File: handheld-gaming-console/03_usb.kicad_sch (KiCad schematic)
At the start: 16 parts, among them U6 USB2514B, Y1 24MHz

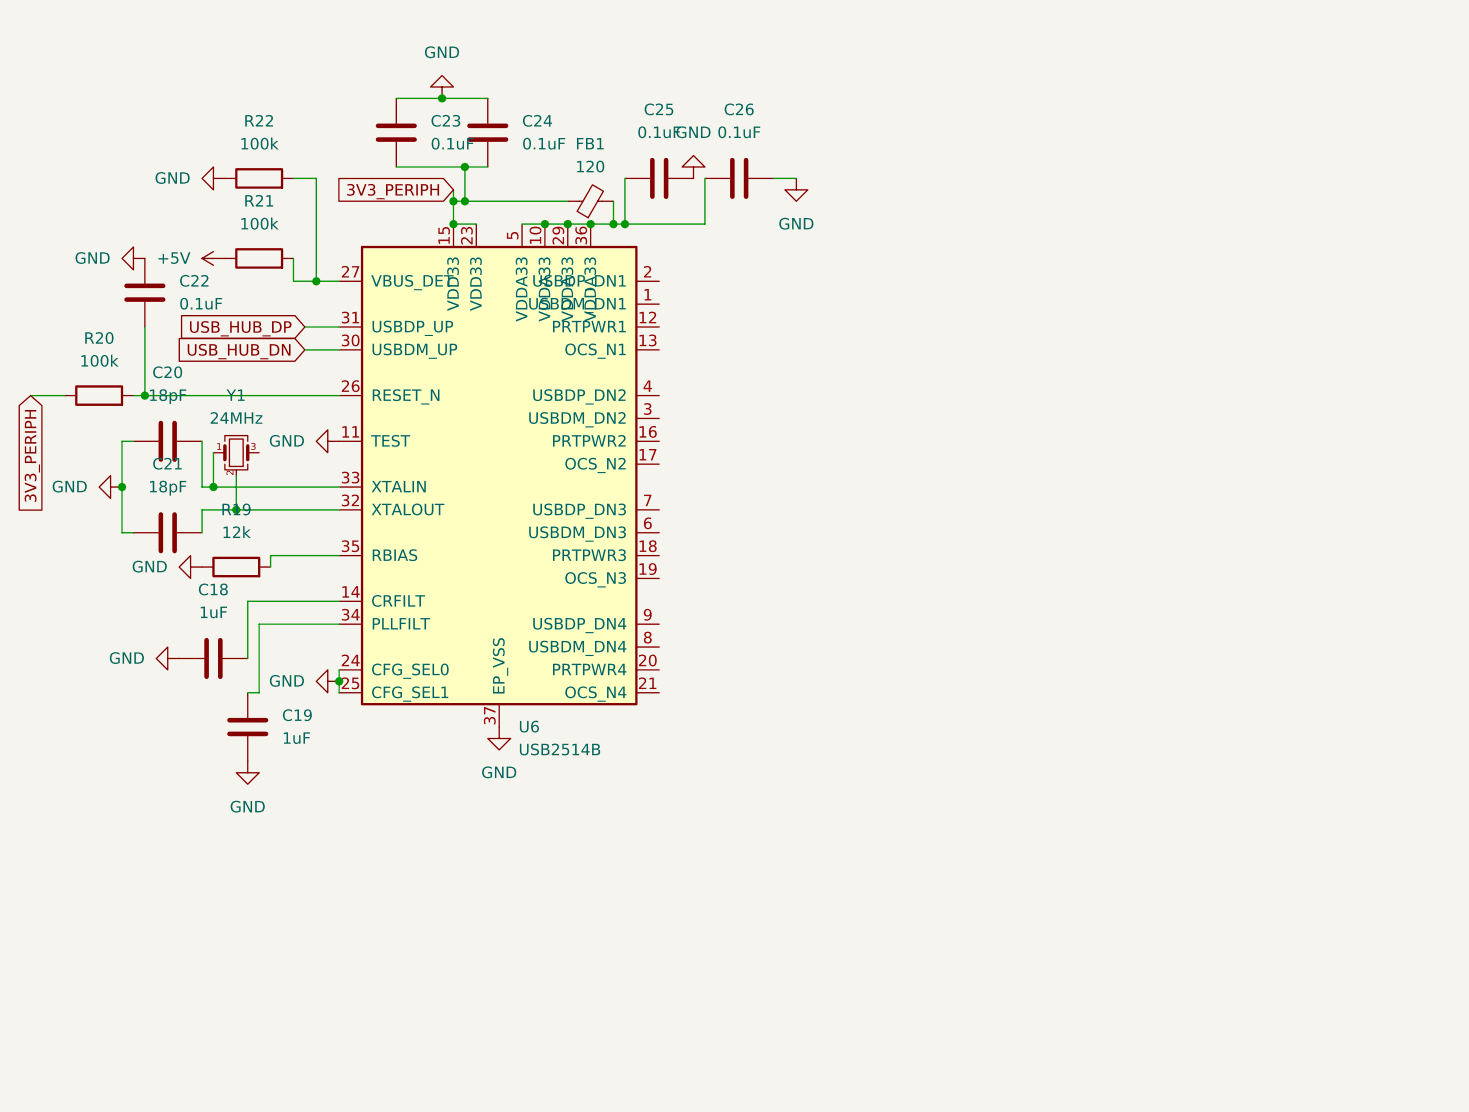
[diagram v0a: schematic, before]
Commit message: feat(usb): complete dual USB-A downstream ports, TPS2051 power switches, and bidirectional ESD protection
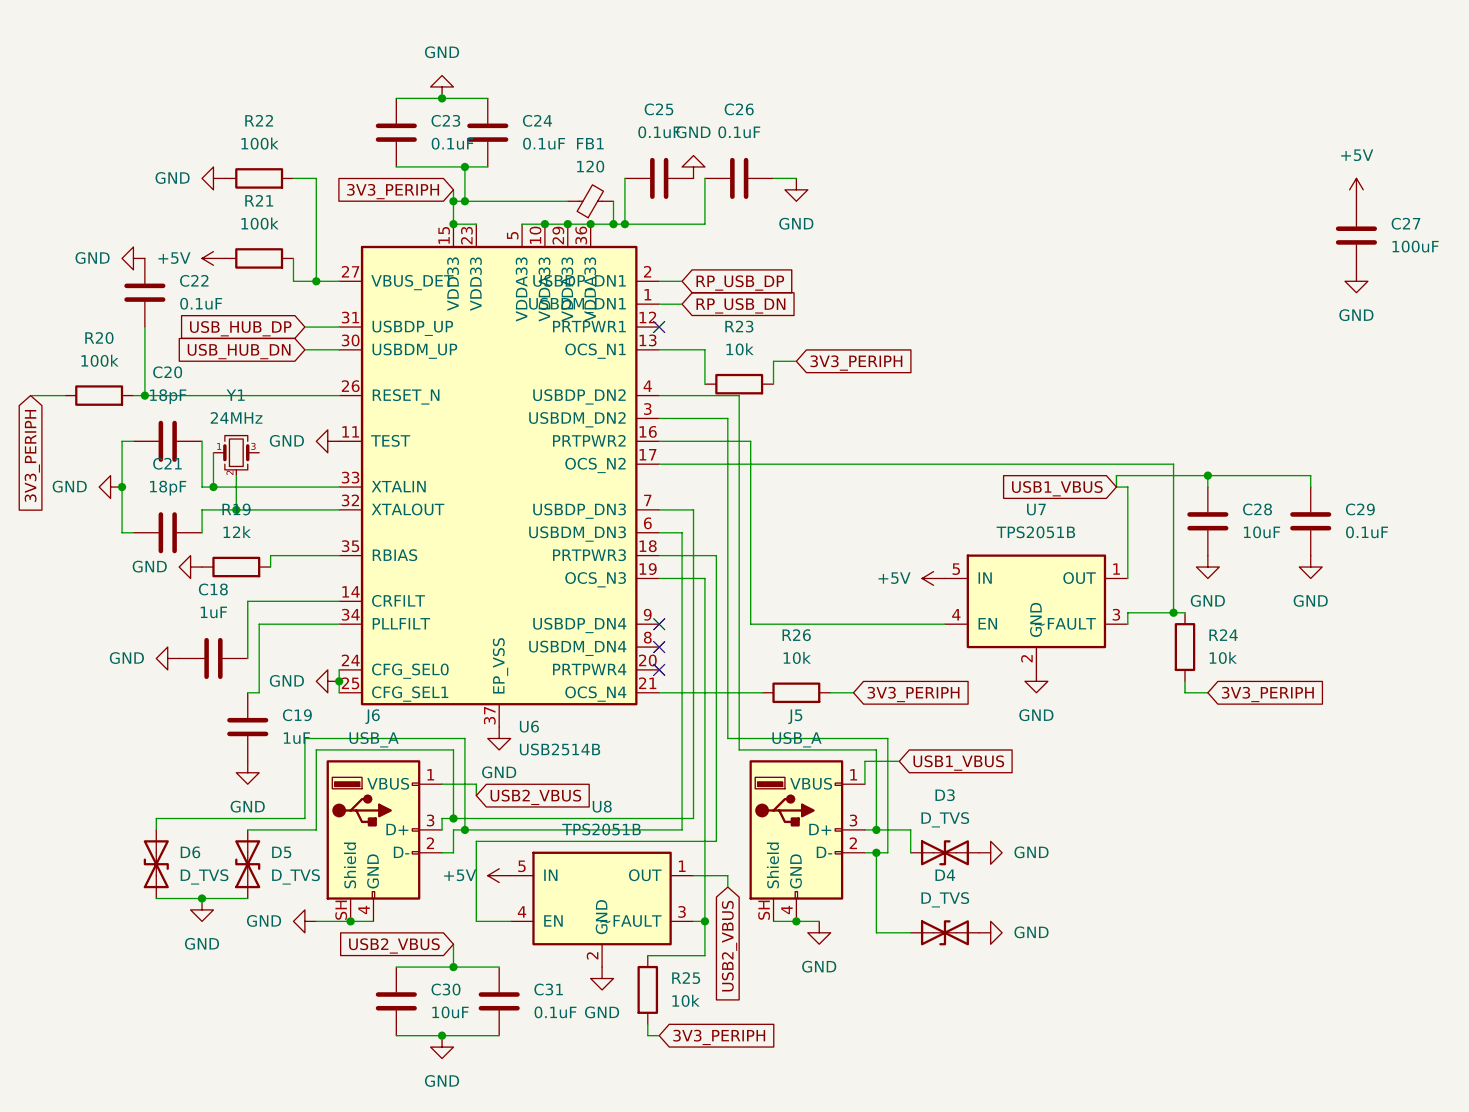
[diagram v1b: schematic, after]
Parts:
- added C27: 100uF, symbol Device:C
- added C28, C30: 10uF, symbol Device:C
- added C29, C31: 0.1uF, symbol Device:C
- added D3, D4, D5, D6: D_TVS, symbol Device:D_TVS
- added J5, J6: USB_A, symbol Connector:USB_A
- added R23, R24, R25, R26: 10k, symbol Device:R
- added U7, U8: TPS2051B, Package_TO_SOT_SMD:SOT-23-5, symbol custom-components:TPS2051B
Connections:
- net +5V: now also C27.1, U7.5 (IN), U8.5 (IN)
- net 3V3_PERIPH: now also R23.2, R24.2, R25.2, R26.2
- net GND: now also C27.2, C28.2, C29.2, C30.2, C31.2, D3.2 (A2), D4.2 (A2), D5.1 (A1), D6.1 (A1), J5.4 (GND), J5.SH (Shield), J6.4 (GND), J6.SH (Shield), U7.2 (GND), U8.2 (GND)
- net RP_USB_DN: now reaches U6.1 (USBDM_DN1)
- net at U6.13 (OCS_N1): now also R23.1
- net at U6.16 (PRTPWR2): now also U7.4 (EN)
- net at U6.17 (OCS_N2): now also R24.1, U7.3 (~FAULT)
- net at U6.18 (PRTPWR3): now also U8.4 (EN)
- net at U6.19 (OCS_N3): now also R25.1, U8.3 (~FAULT)
- net RP_USB_DP: now reaches U6.2 (USBDP_DN1)
- net at U6.21 (OCS_N4): now also R26.1
- net at U6.3 (USBDM_DN2): now also D4.1 (A1), J5.2 (D-)
- net at U6.4 (USBDP_DN2): now also D3.1 (A1), J5.3 (D+)
- net at U6.6 (USBDM_DN3): now also D6.2 (A2), J6.2 (D-)
- net at U6.7 (USBDP_DN3): now also D5.2 (A2), J6.3 (D+)
- new net USB1_VBUS: C28.1, C29.1, J5.1 (VBUS), U7.1 (OUT)
- new net USB2_VBUS: C30.1, C31.1, J6.1 (VBUS), U8.1 (OUT)
- no-connect marks 0 -> 4

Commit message: fix(usb): correct USB2514B reset timing, complete VDDA33 decoupling network, and add TPS2051B VBUS load switch for internal RP2040 port
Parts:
- added C34, C35, C38: 0.1uF, symbol Device:C_Small
- added C36: 1uF, symbol Device:C_Small
- added C37: 10uF, symbol Device:C_Small
- added U9: TPS2051B, Package_TO_SOT_SMD:SOT-23-5, symbol custom-components:TPS2051B
- C22: value 0.1uF -> 1uF
- R20: value 100k -> 10k
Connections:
- net +5V: now also U9.5 (IN)
- net GND: now also C34.2, C35.2, C36.2, C37.2, C38.2, U9.2 (GND)
- net at R23.1, U6.13 (OCS_N1): now also U9.3 (~FAULT)
- net at C25.1, C26.1, FB1.2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: now also C34.1, C35.1, C36.1
- net at U6.12 (PRTPWR1): now also U9.4 (EN)
- new net RP_USB_VBUS: C37.1, C38.1, U9.1 (OUT)
- no-connect marks 4 -> 3
